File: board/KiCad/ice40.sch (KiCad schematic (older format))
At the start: 1 part, among them U1 iCE40_1K4K_TQ144

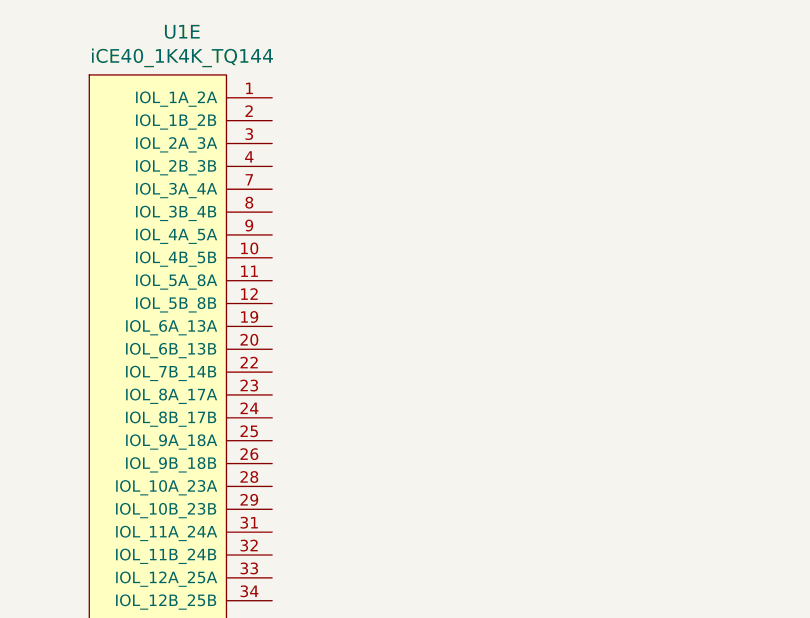
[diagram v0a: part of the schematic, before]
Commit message: First pmod side wiring
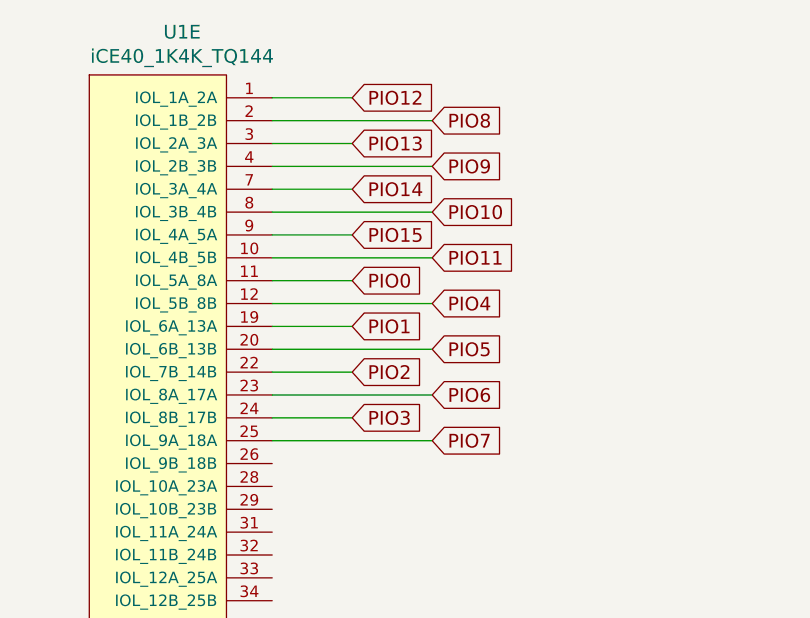
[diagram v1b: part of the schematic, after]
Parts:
- U1: footprint (none) -> Housings_QFP:TQFP-144_20x20mm_Pitch0.5mm
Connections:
- net PIO12: now reaches U1.1 (IOL_1A_2A)
- net PIO11: now reaches U1.10 (IOL_4B_5B)
- net PIO0: now reaches U1.11 (IOL_5A_8A)
- net PIO4: now reaches U1.12 (IOL_5B_8B)
- net PIO1: now reaches U1.19 (IOL_6A_13A)
- net PIO8: now reaches U1.2 (IOL_1B_2B)
- net PIO5: now reaches U1.20 (IOL_6B_13B)
- net PIO2: now reaches U1.22 (IOL_7B_14B)
- net PIO6: now reaches U1.23 (IOL_8A_17A)
- net PIO3: now reaches U1.24 (IOL_8B_17B)
- net PIO7: now reaches U1.25 (IOL_9A_18A)
- net PIO13: now reaches U1.3 (IOL_2A_3A)
- net PIO9: now reaches U1.4 (IOL_2B_3B)
- net PIO14: now reaches U1.7 (IOL_3A_4A)
- net PIO10: now reaches U1.8 (IOL_3B_4B)
- net PIO15: now reaches U1.9 (IOL_4A_5A)
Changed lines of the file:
@@
 LIBS:ice40_1k4k_tq144
 LIBS:myriad
+LIBS:pmod
+LIBS:LMS6002-Pmod-cache
 EELAYER 25 0
 EELAYER END
@@
 F 0 "U1" H 1306 1237 60  0000 C CNN
 F 1 "iCE40_1K4K_TQ144" H 1306 1131 60  0000 C CNN
-F 2 "" H 1500 950 60  0000 C CNN
+F 2 "Housings_QFP:TQFP-144_20x20mm_Pitch0.5mm" H 1500 950 60  0001 C CNN
 F 3 "" H 1500 950 60  0000 C CNN
 	1    1500 950
@@
 F 0 "U1" H 1306 5087 60  0000 C CNN
 F 1 "iCE40_1K4K_TQ144" H 1306 4981 60  0000 C CNN
-F 2 "" H 1500 4800 60  0000 C CNN
+F 2 "Housings_QFP:TQFP-144_20x20mm_Pitch0.5mm" H 1500 4800 60  0001 C CNN
 F 3 "" H 1500 4800 60  0000 C CNN
 	2    1500 4800
@@
 F 0 "U1" H 4306 1237 60  0000 C CNN
 F 1 "iCE40_1K4K_TQ144" H 4306 1131 60  0000 C CNN
-F 2 "" H 4500 950 60  0000 C CNN
+F 2 "Housings_QFP:TQFP-144_20x20mm_Pitch0.5mm" H 4500 950 60  0001 C CNN
 F 3 "" H 4500 950 60  0000 C CNN
 	3    4500 950
@@
 F 0 "U1" H 4306 4137 60  0000 C CNN
 F 1 "iCE40_1K4K_TQ144" H 4306 4031 60  0000 C CNN
-F 2 "" H 4500 3850 60  0000 C CNN
+F 2 "Housings_QFP:TQFP-144_20x20mm_Pitch0.5mm" H 4500 3850 60  0001 C CNN
 F 3 "" H 4500 3850 60  0000 C CNN
 	4    4500 3850
@@
 F 0 "U1" H 10306 4487 60  0000 C CNN
 F 1 "iCE40_1K4K_TQ144" H 10306 4381 60  0000 C CNN
-F 2 "" H 10500 4200 60  0000 C CNN
+F 2 "Housings_QFP:TQFP-144_20x20mm_Pitch0.5mm" H 10500 4200 60  0001 C CNN
 F 3 "" H 10500 4200 60  0000 C CNN
 	6    10500 4200
@@
 F 0 "U1" H 7856 1187 60  0000 C CNN
 F 1 "iCE40_1K4K_TQ144" H 7856 1081 60  0000 C CNN
-F 2 "" H 8050 900 60  0000 C CNN
+F 2 "Housings_QFP:TQFP-144_20x20mm_Pitch0.5mm" H 8050 900 60  0001 C CNN
 F 3 "" H 8050 900 60  0000 C CNN
 	5    8050 900
 	1    0    0    -1
 $EndComp
+Text GLabel 8600 900  2    60   Input ~ 0
+PIO12
+Text GLabel 8950 1000 2    60   Input ~ 0
+PIO8
+Text GLabel 8600 1100 2    60   Input ~ 0
+PIO13
+Wire Wire Line
+	8950 1000 8250 1000
+Wire Wire Line
+	8250 900  8600 900
+Wire Wire Line
+	8600 1100 8250 1100
+Text GLabel 8950 1200 2    60   Input ~ 0
+PIO9
+Text GLabel 8950 1400 2    60   Input ~ 0
+PIO10
+Text GLabel 8950 1600 2    60   Input ~ 0
+PIO11
+Text GLabel 8600 1300 2    60   Input ~ 0
+PIO14
+Text GLabel 8600 1500 2    60   Input ~ 0
+PIO15
+Wire Wire Line
+	8950 1200 8250 1200
+Wire Wire Line
+	8250 1300 8600 1300
+Wire Wire Line
+	8600 1500 8250 1500
+Wire Wire Line
+	8250 1400 8950 1400
+Wire Wire Line
+	8950 1600 8250 1600
+Text GLabel 8600 1700 2    60   Input ~ 0
+PIO0
+Text GLabel 8600 1900 2    60   Input ~ 0
+PIO1
+Text GLabel 8600 2100 2    60   Input ~ 0
+PIO2
+Text GLabel 8600 2300 2    60   Input ~ 0
+PIO3
+Text GLabel 8950 1800 2    60   Input ~ 0
+PIO4
+Text GLabel 8950 2000 2    60   Input ~ 0
+PIO5
+Text GLabel 8950 2200 2    60   Input ~ 0
+PIO6
+Text GLabel 8950 2400 2    60   Input ~ 0
+PIO7
+Wire Wire Line
+	8250 1700 8600 1700
+Wire Wire Line
+	8250 1800 8950 1800
+Wire Wire Line
+	8950 2000 8250 2000
+Wire Wire Line
+	8250 1900 8600 1900
+Wire Wire Line
+	8600 2100 8250 2100
+Wire Wire Line
+	8250 2200 8950 2200
+Wire Wire Line
+	8950 2400 8250 2400
+Wire Wire Line
+	8250 2300 8600 2300
 $EndSCHEMATC

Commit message: pmod wiring
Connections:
- net +3V3: now reaches U1.30 (VCCIO_3)
- net +3V3: now also U1.6 (VCCIO_3)
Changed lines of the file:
@@
 Wire Wire Line
 	8250 2300 8600 2300
+Wire Wire Line
+	1700 3750 1850 3750
+Wire Wire Line
+	1850 3750 1850 3650
+Wire Wire Line
+	1850 3650 1700 3650
+Wire Wire Line
+	1850 3700 2050 3700
+Connection ~ 1850 3700
+$Comp
+L +3V3 #PWR1
+U 1 1 56A62583
+P 2050 3700
+F 0 "#PWR1" H 2050 3550 50  0001 C CNN
+F 1 "+3V3" H 2068 3874 50  0000 C CNN
+F 2 "" H 2050 3700 50  0000 C CNN
+F 3 "" H 2050 3700 50  0000 C CNN
+	1    2050 3700
+	1    0    0    -1
+$EndComp
 $EndSCHEMATC

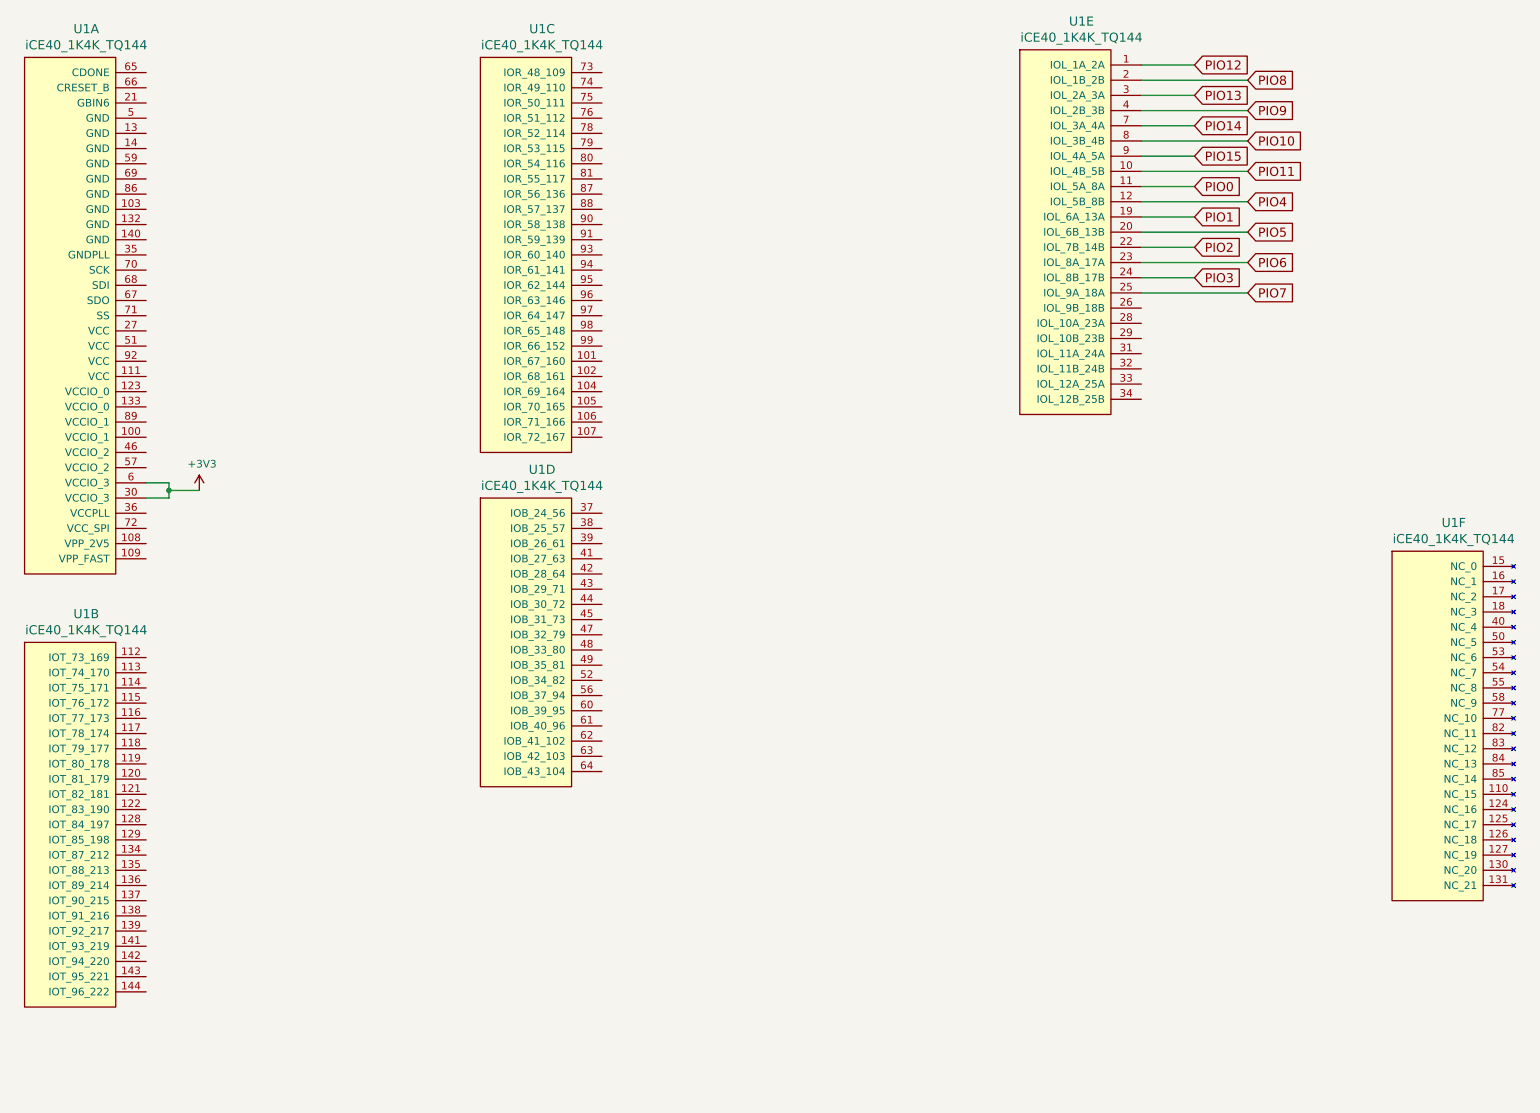
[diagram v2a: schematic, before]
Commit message: 1.2V power supply
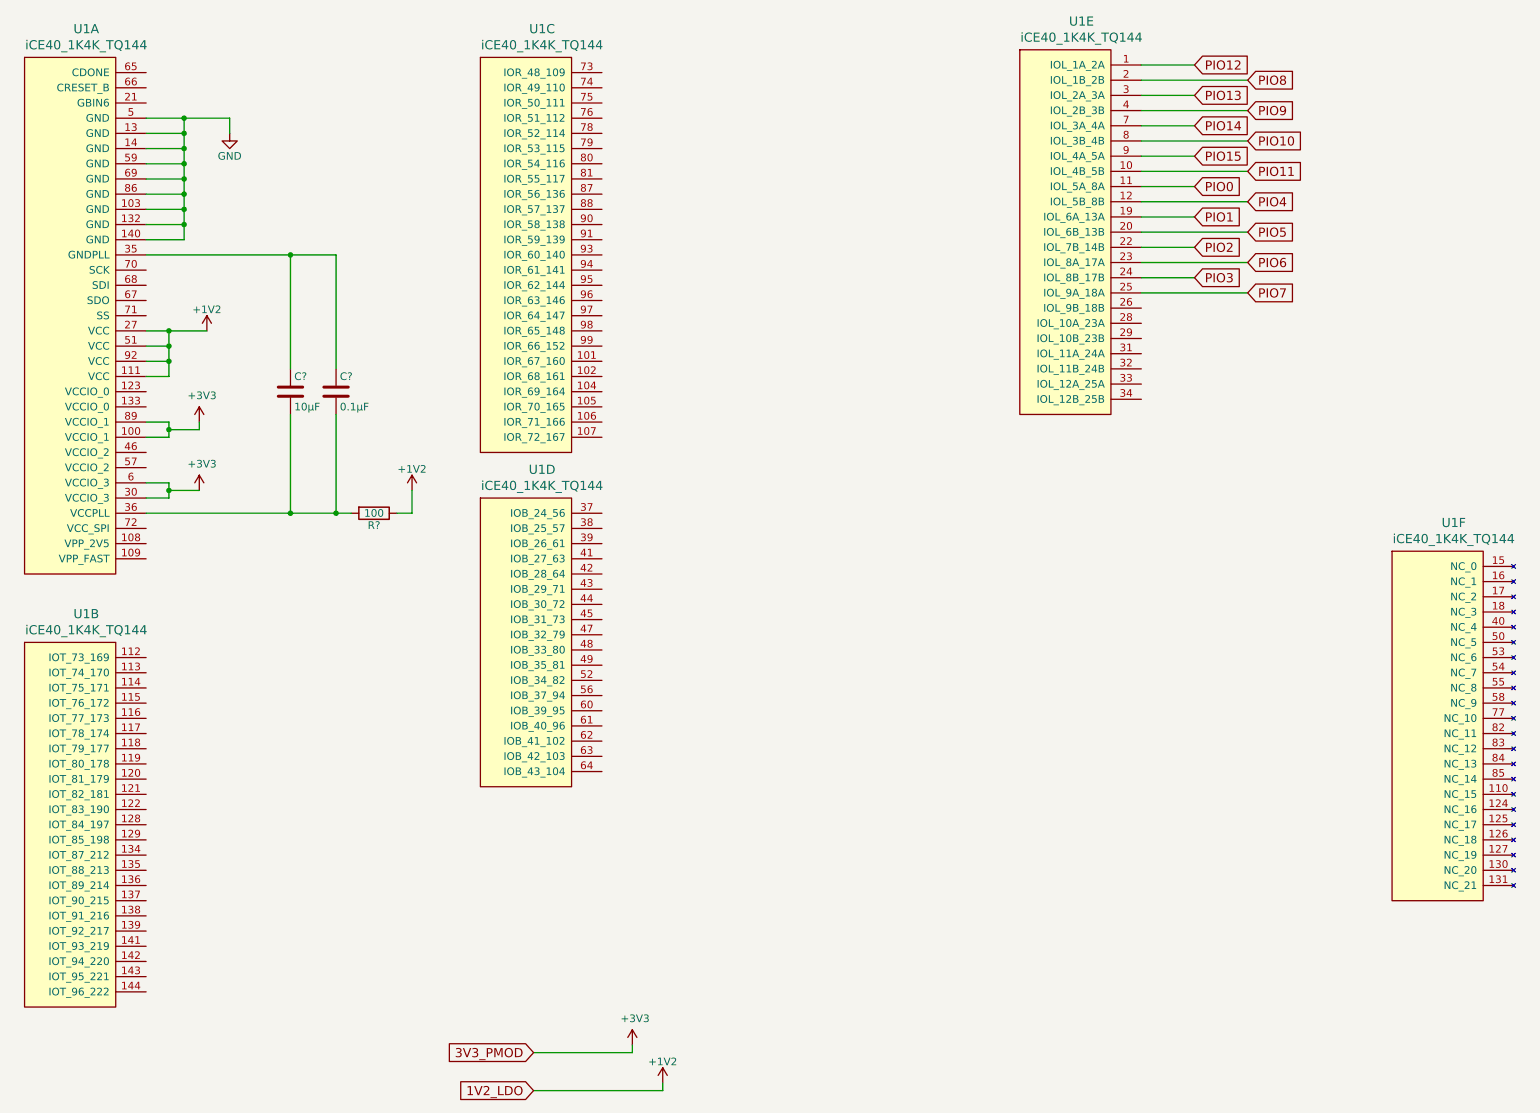
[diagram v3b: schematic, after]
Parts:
- added C?: 10µF, symbol C
- added C?: 0.1µF, symbol C
- added R?: 100, symbol R
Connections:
- net +3V3: now also U1.100 (VCCIO_1), U1.89 (VCCIO_1)
- net GND: now reaches U1.103 (GND)
- net GND: now also U1.13 (GND), U1.132 (GND), U1.14 (GND), U1.140 (GND), U1.5 (GND), U1.59 (GND), U1.69 (GND), U1.86 (GND)
- net +1V2: now reaches U1.111 (VCC)
- net +1V2: now also U1.27 (VCC), U1.51 (VCC), U1.92 (VCC), R?.1
- net at U1.35 (GNDPLL): now also C?.1, C?.1
- net at U1.36 (VCCPLL): now also C?.2, C?.2, R?.2
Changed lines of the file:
@@
 EESchema Schematic File Version 2
+LIBS:LMS6002-Pmod-rescue
 LIBS:power
 LIBS:device
@@
 $Descr A4 11693 8268
 encoding utf-8
-Sheet 3 4
+Sheet 3 5
 Title ""
 Date ""
@@
 Text GLabel 8600 1100 2    60   Input ~ 0
 PIO13
-Wire Wire Line
-	8950 1000 8250 1000
-Wire Wire Line
-	8250 900  8600 900
-Wire Wire Line
-	8600 1100 8250 1100
 Text GLabel 8950 1200 2    60   Input ~ 0
 PIO9
@@
 Text GLabel 8600 1500 2    60   Input ~ 0
 PIO15
-Wire Wire Line
-	8950 1200 8250 1200
-Wire Wire Line
-	8250 1300 8600 1300
-Wire Wire Line
-	8600 1500 8250 1500
-Wire Wire Line
-	8250 1400 8950 1400
-Wire Wire Line
-	8950 1600 8250 1600
 Text GLabel 8600 1700 2    60   Input ~ 0
 PIO0
@@
 Text GLabel 8950 2400 2    60   Input ~ 0
 PIO7
-Wire Wire Line
-	8250 1700 8600 1700
-Wire Wire Line
-	8250 1800 8950 1800
-Wire Wire Line
-	8950 2000 8250 2000
-Wire Wire Line
-	8250 1900 8600 1900
-Wire Wire Line
-	8600 2100 8250 2100
-Wire Wire Line
-	8250 2200 8950 2200
-Wire Wire Line
-	8950 2400 8250 2400
-Wire Wire Line
-	8250 2300 8600 2300
-Wire Wire Line
-	1700 3750 1850 3750
-Wire Wire Line
-	1850 3750 1850 3650
-Wire Wire Line
-	1850 3650 1700 3650
-Wire Wire Line
-	1850 3700 2050 3700
-Connection ~ 1850 3700
-$Comp
-L +3V3 #PWR1
+$Comp
+L +3V3 #PWR5
 U 1 1 56A62583
 P 2050 3700
-F 0 "#PWR1" H 2050 3550 50  0001 C CNN
+F 0 "#PWR5" H 2050 3550 50  0001 C CNN
 F 1 "+3V3" H 2068 3874 50  0000 C CNN
 F 2 "" H 2050 3700 50  0000 C CNN
@@
 	1    0    0    -1
 $EndComp
+Text GLabel 4250 7400 0    60   Input ~ 0
+3V3_PMOD
+$Comp
+L +3V3 #PWR?
+U 1 1 56ABB1F6
+P 4900 7350
+F 0 "#PWR?" H 4900 7200 50  0001 C CNN
+F 1 "+3V3" H 4918 7524 50  0000 C CNN
+F 2 "" H 4900 7350 50  0000 C CNN
+F 3 "" H 4900 7350 50  0000 C CNN
+	1    4900 7350
+	1    0    0    -1
+$EndComp
+Text GLabel 4250 7650 0    60   Input ~ 0
+1V2_LDO
+$Comp
+L +1V2 #PWR?
+U 1 1 56ABBB92
+P 5100 7600
+F 0 "#PWR?" H 5100 7450 50  0001 C CNN
+F 1 "+1V2" H 5100 7740 50  0000 C CNN
+F 2 "" H 5100 7600 60  0000 C CNN
+F 3 "" H 5100 7600 60  0000 C CNN
+	1    5100 7600
+	1    0    0    -1
+$EndComp
+$Comp
+L +1V2 #PWR?
+U 1 1 56ABC35C
+P 2100 2650
+F 0 "#PWR?" H 2100 2500 50  0001 C CNN
+F 1 "+1V2" H 2100 2790 50  0000 C CNN
+F 2 "" H 2100 2650 60  0000 C CNN
+F 3 "" H 2100 2650 60  0000 C CNN
+	1    2100 2650
+	1    0    0    -1
+$EndComp
+$Comp
+L +1V2 #PWR?
+U 1 1 56ABC562
+P 3450 3700
+F 0 "#PWR?" H 3450 3550 50  0001 C CNN
+F 1 "+1V2" H 3450 3840 50  0000 C CNN
+F 2 "" H 3450 3700 60  0000 C CNN
+F 3 "" H 3450 3700 60  0000 C CNN
+	1    3450 3700
+	1    0    0    -1
+$EndComp
+$Comp
+L C C?
+U 1 1 56ABC765
+P 2650 3050
+F 0 "C?" H 2675 3150 50  0000 L CNN
+F 1 "10µF" H 2675 2950 50  0000 L CNN
+F 2 "" H 2688 2900 30  0000 C CNN
+F 3 "" H 2650 3050 60  0000 C CNN
+	1    2650 3050
+	1    0    0    -1
+$EndComp
+$Comp
+L C C?
+U 1 1 56ABC7CC
+P 2950 3050
+F 0 "C?" H 2975 3150 50  0000 L CNN
+F 1 "0.1µF" H 2975 2950 50  0000 L CNN
+F 2 "" H 2988 2900 30  0000 C CNN
+F 3 "" H 2950 3050 60  0000 C CNN
+	1    2950 3050
+	1    0    0    -1
+$EndComp
+$Comp
+L R R?
+U 1 1 56ABD0CF
+P 3200 3850
+F 0 "R?" V 3280 3850 50  0000 C CNN
+F 1 "100" V 3200 3850 50  0000 C CNN
+F 2 "" V 3130 3850 30  0000 C CNN
+F 3 "" H 3200 3850 30  0000 C CNN
+	1    3200 3850
+	0    1    1    0
+$EndComp
+Wire Wire Line
+	8950 1000 8250 1000
+Wire Wire Line
+	8250 900  8600 900
+Wire Wire Line
+	8600 1100 8250 1100
+Wire Wire Line
+	8950 1200 8250 1200
+Wire Wire Line
+	8250 1300 8600 1300
+Wire Wire Line
+	8600 1500 8250 1500
+Wire Wire Line
+	8250 1400 8950 1400
+Wire Wire Line
+	8950 1600 8250 1600
+Wire Wire Line
+	8250 1700 8600 1700
+Wire Wire Line
+	8250 1800 8950 1800
+Wire Wire Line
+	8950 2000 8250 2000
+Wire Wire Line
+	8250 1900 8600 1900
+Wire Wire Line
+	8600 2100 8250 2100
+Wire Wire Line
+	8250 2200 8950 2200
+Wire Wire Line
+	8950 2400 8250 2400
+Wire Wire Line
+	8250 2300 8600 2300
+Wire Wire Line
+	1700 3750 1850 3750
+Wire Wire Line
+	1850 3750 1850 3650
+Wire Wire Line
+	1850 3650 1700 3650
+Wire Wire Line
+	1850 3700 2050 3700
+Connection ~ 1850 3700
+Wire Wire Line
+	4250 7400 4900 7400
+Wire Wire Line
+	4900 7400 4900 7350
+Wire Wire Line
+	4250 7650 5100 7650
+Wire Wire Line
+	5100 7650 5100 7600
+Wire Wire Line
+	1700 2650 2100 2650
+Wire Wire Line
+	1850 2650 1850 2950
+Wire Wire Line
+	1850 2950 1700 2950
+Wire Wire Line
+	1700 2850 1850 2850
+Connection ~ 1850 2850
+Wire Wire Line
+	1700 2750 1850 2750
+Connection ~ 1850 2750
+Connection ~ 1850 2650
+Wire Wire Line
+	3450 3850 3450 3700
+Wire Wire Line
+	2650 3200 2650 3850
+Connection ~ 2650 3850
+Wire Wire Line
+	2950 3850 2950 3200
+Connection ~ 2950 3850
+Wire Wire Line
+	1700 2150 2950 2150
+Wire Wire Line
+	2650 2150 2650 2900
+Wire Wire Line
+	2950 2150 2950 2900
+Connection ~ 2650 2150
+Wire Wire Line
+	1700 3850 3050 3850
+Wire Wire Line
+	3350 3850 3450 3850
+Wire Wire Line
+	1700 2050 1950 2050
+Wire Wire Line
+	1950 2050 1950 1250
+Wire Wire Line
+	1700 1250 2250 1250
+Wire Wire Line
+	1700 1350 1950 1350
+Connection ~ 1950 1350
+Wire Wire Line
+	1700 1450 1950 1450
+Connection ~ 1950 1450
+Wire Wire Line
+	1700 1550 1950 1550
+Connection ~ 1950 1550
+Wire Wire Line
+	1700 1650 1950 1650
+Connection ~ 1950 1650
+Wire Wire Line
+	1700 1750 1950 1750
+Connection ~ 1950 1750
+Wire Wire Line
+	1700 1850 1950 1850
+Connection ~ 1950 1850
+Wire Wire Line
+	1700 1950 1950 1950
+Connection ~ 1950 1950
+Wire Wire Line
+	1700 3250 1850 3250
+Wire Wire Line
+	1850 3250 1850 3350
+Wire Wire Line
+	1850 3350 1700 3350
+$Comp
+L +3V3 #PWR?
+U 1 1 56ABE3D7
+P 2050 3250
+F 0 "#PWR?" H 2050 3100 50  0001 C CNN
+F 1 "+3V3" H 2068 3424 50  0000 C CNN
+F 2 "" H 2050 3250 50  0000 C CNN
+F 3 "" H 2050 3250 50  0000 C CNN
+	1    2050 3250
+	1    0    0    -1
+$EndComp
+Wire Wire Line
+	1850 3300 2050 3300
+Wire Wire Line
+	2050 3300 2050 3250
+Connection ~ 1850 3300
+$Comp
+L GND #PWR?
+U 1 1 56ABE688
+P 2250 1350
+F 0 "#PWR?" H 2250 1100 50  0001 C CNN
+F 1 "GND" H 2250 1200 50  0000 C CNN
+F 2 "" H 2250 1350 60  0000 C CNN
+F 3 "" H 2250 1350 60  0000 C CNN
+	1    2250 1350
+	1    0    0    -1
+$EndComp
+Wire Wire Line
+	2250 1250 2250 1350
+Connection ~ 1950 1250
 $EndSCHEMATC

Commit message: removed legacy footprints
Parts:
- gave numbers to parts that had none: 3
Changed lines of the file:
@@
 PIO7
 $Comp
-L +3V3 #PWR5
+L +3V3 #PWR6
 U 1 1 56A62583
 P 2050 3700
-F 0 "#PWR5" H 2050 3550 50  0001 C CNN
+F 0 "#PWR6" H 2050 3550 50  0001 C CNN
 F 1 "+3V3" H 2068 3874 50  0000 C CNN
 F 2 "" H 2050 3700 50  0000 C CNN
@@
 3V3_PMOD
 $Comp
-L +3V3 #PWR?
+L +3V3 #PWR10
 U 1 1 56ABB1F6
 P 4900 7350
-F 0 "#PWR?" H 4900 7200 50  0001 C CNN
+F 0 "#PWR10" H 4900 7200 50  0001 C CNN
 F 1 "+3V3" H 4918 7524 50  0000 C CNN
 F 2 "" H 4900 7350 50  0000 C CNN
@@
 1V2_LDO
 $Comp
-L +1V2 #PWR?
+L +1V2 #PWR11
 U 1 1 56ABBB92
 P 5100 7600
-F 0 "#PWR?" H 5100 7450 50  0001 C CNN
+F 0 "#PWR11" H 5100 7450 50  0001 C CNN
 F 1 "+1V2" H 5100 7740 50  0000 C CNN
 F 2 "" H 5100 7600 60  0000 C CNN
@@
 $EndComp
 $Comp
-L +1V2 #PWR?
+L +1V2 #PWR7
 U 1 1 56ABC35C
 P 2100 2650
-F 0 "#PWR?" H 2100 2500 50  0001 C CNN
+F 0 "#PWR7" H 2100 2500 50  0001 C CNN
 F 1 "+1V2" H 2100 2790 50  0000 C CNN
 F 2 "" H 2100 2650 60  0000 C CNN
@@
 $EndComp
 $Comp
-L +1V2 #PWR?
+L +1V2 #PWR9
 U 1 1 56ABC562
 P 3450 3700
-F 0 "#PWR?" H 3450 3550 50  0001 C CNN
+F 0 "#PWR9" H 3450 3550 50  0001 C CNN
 F 1 "+1V2" H 3450 3840 50  0000 C CNN
 F 2 "" H 3450 3700 60  0000 C CNN
@@
 $EndComp
 $Comp
-L C C?
+L C C1
 U 1 1 56ABC765
 P 2650 3050
-F 0 "C?" H 2675 3150 50  0000 L CNN
+F 0 "C1" H 2675 3150 50  0000 L CNN
 F 1 "10µF" H 2675 2950 50  0000 L CNN
-F 2 "" H 2688 2900 30  0000 C CNN
+F 2 "" H 2688 2900 30  0001 C CNN
 F 3 "" H 2650 3050 60  0000 C CNN
 	1    2650 3050
@@
 $EndComp
 $Comp
-L C C?
+L C C2
 U 1 1 56ABC7CC
 P 2950 3050
-F 0 "C?" H 2975 3150 50  0000 L CNN
+F 0 "C2" H 2975 3150 50  0000 L CNN
 F 1 "0.1µF" H 2975 2950 50  0000 L CNN
-F 2 "" H 2988 2900 30  0000 C CNN
+F 2 "" H 2988 2900 30  0001 C CNN
 F 3 "" H 2950 3050 60  0000 C CNN
 	1    2950 3050
@@
 $EndComp
 $Comp
-L R R?
+L R R1
 U 1 1 56ABD0CF
 P 3200 3850
-F 0 "R?" V 3280 3850 50  0000 C CNN
+F 0 "R1" V 3280 3850 50  0000 C CNN
 F 1 "100" V 3200 3850 50  0000 C CNN
-F 2 "" V 3130 3850 30  0000 C CNN
+F 2 "" V 3130 3850 30  0001 C CNN
 F 3 "" H 3200 3850 30  0000 C CNN
 	1    3200 3850
@@
 	1850 3350 1700 3350
 $Comp
-L +3V3 #PWR?
+L +3V3 #PWR5
 U 1 1 56ABE3D7
 P 2050 3250
-F 0 "#PWR?" H 2050 3100 50  0001 C CNN
+F 0 "#PWR5" H 2050 3100 50  0001 C CNN
 F 1 "+3V3" H 2068 3424 50  0000 C CNN
 F 2 "" H 2050 3250 50  0000 C CNN
@@
 Connection ~ 1850 3300
 $Comp
-L GND #PWR?
+L GND #PWR8
 U 1 1 56ABE688
 P 2250 1350
-F 0 "#PWR?" H 2250 1100 50  0001 C CNN
+F 0 "#PWR8" H 2250 1100 50  0001 C CNN
 F 1 "GND" H 2250 1200 50  0000 C CNN
 F 2 "" H 2250 1350 60  0000 C CNN
